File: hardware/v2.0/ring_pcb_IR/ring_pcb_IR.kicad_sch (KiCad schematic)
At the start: 22 parts, among them Q1 Q_PNP_BEC, Q2 Q_Dual_NPN_NPN_E1B1C2E2B2C1, Q3 Q_Dual_NPN_NPN_E1B1C2E2B2C1, U2 ATtiny85-20M

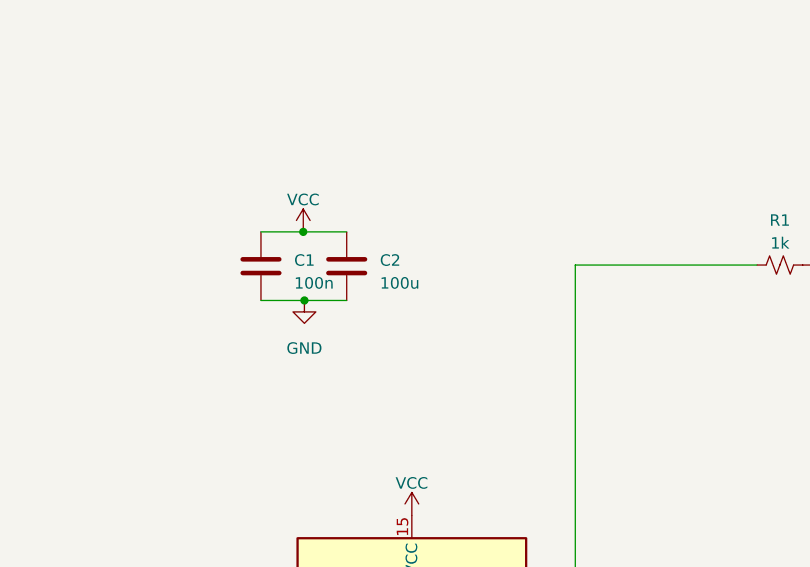
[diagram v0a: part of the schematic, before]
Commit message: New Gerbers with smaller dual-NPN
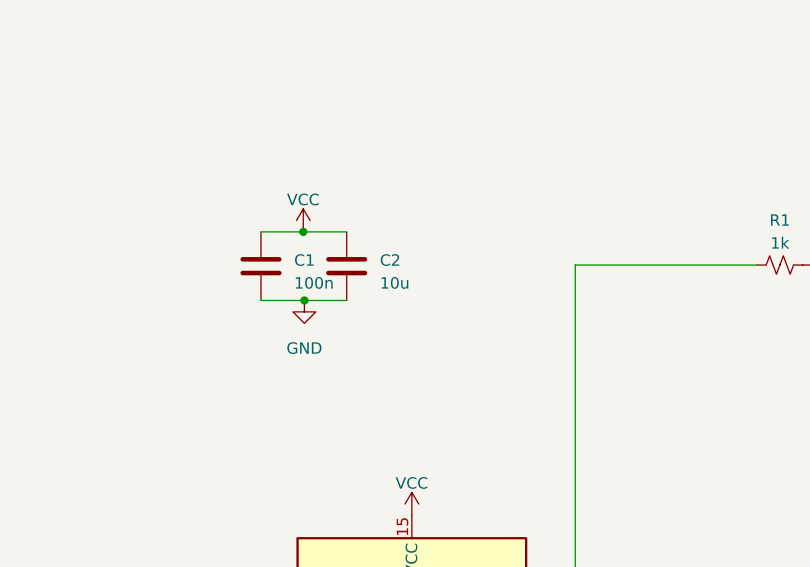
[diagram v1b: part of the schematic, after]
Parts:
- C2: value 100u -> 10u; MPN (none) -> GRM188R61A106KE69J
- Q1: MPN (none) -> MMBTA55LT1G
- TP1, TP2, TP3, TP4, TP5, TP6, TP7, TP8, TP9: MPN (none) -> DNP
- U2: MPN (none) -> ATTINY85-20MU
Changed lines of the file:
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@@
       (effects (font (size 1.27 1.27)) hide)
     )
-    (property "MPN" "" (at 87.249 138.557 0)
+    (property "MPN" "DNP" (at 87.249 138.557 0)
       (effects (font (size 1.27 1.27)) hide)
     )
@@
       (effects (font (size 1.27 1.27)) hide)
     )
-    (property "MPN" "" (at 108.839 138.43 0)
+    (property "MPN" "DNP" (at 108.839 138.43 0)
       (effects (font (size 1.27 1.27)) hide)
     )
@@
       (effects (font (size 1.27 1.27)) hide)
     )
-    (property "MPN" "" (at 87.503 147.32 0)
+    (property "MPN" "DNP" (at 87.503 147.32 0)
       (effects (font (size 1.27 1.27)) hide)
     )
@@
       (effects (font (size 1.27 1.27)) hide)
     )
-    (property "MPN" "" (at 101.473 138.43 0)
+    (property "MPN" "DNP" (at 101.473 138.43 0)
       (effects (font (size 1.27 1.27)) hide)
     )
@@
       (effects (font (size 1.27 1.27)) hide)
     )
-    (property "MPN" "" (at 112.395 103.886 0)
+    (property "MPN" "ATTINY85-20MU" (at 112.395 103.886 0)
       (effects (font (size 1.27 1.27)) hide)
     )
@@
       (effects (font (size 1.27 1.27)) hide)
     )
-    (property "MPN" "" (at 104.013 147.447 0)
+    (property "MPN" "DNP" (at 104.013 147.447 0)
       (effects (font (size 1.27 1.27)) hide)
     )
@@
       (effects (font (size 1.27 1.27)) hide)
     )
-    (property "MPN" "" (at 73.406 138.684 0)
+    (property "MPN" "DNP" (at 73.406 138.684 0)
       (effects (font (size 1.27 1.27)) hide)
     )
@@
       (effects (font (size 1.27 1.27)) (justify left))
     )
-    (property "Value" "100u" (at 108.839 62.865 0)
+    (property "Value" "10u" (at 108.839 62.865 0)
       (effects (font (size 1.27 1.27)) (justify left))
     )
@@
       (effects (font (size 1.27 1.27)) hide)
     )
-    (property "Datasheet" "~" (at 105.156 60.96 0)
-      (effects (font (size 1.27 1.27)) hide)
-    )
-    (property "MPN" "" (at 105.156 60.96 0)
+    (property "Datasheet" "https://au.mouser.com/datasheet/2/281/murata_03052018_GRM_Series_1-1310166.pdf" (at 105.156 60.96 0)
+      (effects (font (size 1.27 1.27)) hide)
+    )
+    (property "MPN" "GRM188R61A106KE69J" (at 105.156 60.96 0)
       (effects (font (size 1.27 1.27)) hide)
     )
@@
       (effects (font (size 1.27 1.27)) hide)
     )
-    (property "MPN" "" (at 58.928 147.066 0)
+    (property "MPN" "DNP" (at 58.928 147.066 0)
       (effects (font (size 1.27 1.27)) hide)
     )
@@
       (effects (font (size 1.27 1.27)) hide)
     )
-    (property "MPN" "" (at 73.406 147.32 0)
+    (property "MPN" "DNP" (at 73.406 147.32 0)
       (effects (font (size 1.27 1.27)) hide)
     )
@@
       (effects (font (size 1.27 1.27)) hide)
     )
-    (property "MPN" "" (at 59.055 138.938 0)
+    (property "MPN" "DNP" (at 59.055 138.938 0)
       (effects (font (size 1.27 1.27)) hide)
     )
@@
       (effects (font (size 1.27 1.27)) hide)
     )
-    (property "Datasheet" "~" (at 160.909 60.833 0)
-      (effects (font (size 1.27 1.27)) hide)
-    )
-    (property "MPN" "" (at 160.909 60.833 0)
-      (effects (font (size 1.27 1.27)) hide)
-    )
+    (property "Datasheet" "https://au.mouser.com/datasheet/2/308/1/MMBTA55LT1_D-2316071.pdf" (at 160.909 60.833 0)
+      (effects (font (size 1.27 1.27)) hide)
+    )
+    (property "MPN" "MMBTA55LT1G" (at 160.909 60.833 0)
+      (effects (font (size 1.27 1.27)) hide)
+    )

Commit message: Create BOM
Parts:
- TP1, TP2, TP3, TP4, TP5, TP6, TP7, TP8, TP9: DNP (none) -> DNP
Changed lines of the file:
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@@
+      (effects (font (size 1.27 1.27)) hide)
+    )
+    (property "DNP" "" (at 223.4692 29.2608 0)
       (effects (font (size 1.27 1.27)) hide)
     )
@@
       (effects (font (size 1.27 1.27)) hide)
     )
+    (property "DNP" "DNP" (at 87.249 138.557 0)
+      (effects (font (size 1.27 1.27)) hide)
+    )
     (pin "1")
     (instances
@@
       (effects (font (size 1.27 1.27)) hide)
     )
+    (property "DNP" "" (at 95.631 60.96 0)
+      (effects (font (size 1.27 1.27)) hide)
+    )
     (pin "1")
     (pin "2")
@@
       (effects (font (size 1.27 1.27)) hide)
     )
+    (property "DNP" "DNP" (at 108.839 138.43 0)
+      (effects (font (size 1.27 1.27)) hide)
+    )
     (pin "1")
     (instances
@@
       (effects (font (size 1.27 1.27)) hide)
     )
+    (property "DNP" "DNP" (at 87.503 147.32 0)
+      (effects (font (size 1.27 1.27)) hide)
+    )
     (pin "1")
     (instances
@@
       (effects (font (size 1.27 1.27)) hide)
     )
+    (property "DNP" "" (at 179.07 120.65 0)
+      (effects (font (size 1.27 1.27)) hide)
+    )
     (pin "1")
     (pin "2")
@@
     )
     (property "MPN" "BC847BS,115" (at 195.707 45.847 0)
+      (effects (font (size 1.27 1.27)) hide)
+    )
+    (property "DNP" "" (at 195.707 45.847 0)
       (effects (font (size 1.27 1.27)) hide)
     )
@@
       (effects (font (size 1.27 1.27)) hide)
     )
+    (property "DNP" "DNP" (at 101.473 138.43 0)
+      (effects (font (size 1.27 1.27)) hide)
+    )
     (pin "1")
     (instances
@@
     )
     (property "MPN" "ATTINY85-20MU" (at 112.395 103.886 0)
+      (effects (font (size 1.27 1.27)) hide)
+    )
+    (property "DNP" "" (at 112.395 103.886 0)
       (effects (font (size 1.27 1.27)) hide)
     )
@@
       (effects (font (size 1.27 1.27)) hide)
     )
+    (property "DNP" "" (at 220.853 45.593 0)
+      (effects (font (size 1.27 1.27)) hide)
+    )
     (pin "1")
     (pin "2")
@@
       (effects (font (size 1.27 1.27)) hide)
     )
+    (property "DNP" "" (at 153.289 60.833 0)
+      (effects (font (size 1.27 1.27)) hide)
+    )
     (pin "1")
     (pin "2")
@@
       (effects (font (size 1.27 1.27)) hide)
     )
+    (property "DNP" "DNP" (at 104.013 147.447 0)
+      (effects (font (size 1.27 1.27)) hide)
+    )
     (pin "1")
     (instances
@@
       (effects (font (size 1.27 1.27)) hide)
     )
+    (property "DNP" "" (at 198.1708 29.2608 0)
+      (effects (font (size 1.27 1.27)) hide)
+    )
     (pin "1")
     (pin "2")
@@
       (effects (font (size 1.27 1.27)) hide)
     )
+    (property "DNP" "DNP" (at 73.406 138.684 0)
+      (effects (font (size 1.27 1.27)) hide)
+    )
     (pin "1")
     (instances
@@
       (effects (font (size 1.27 1.27)) hide)
     )
+    (property "DNP" "" (at 223.4692 87.7824 0)
+      (effects (font (size 1.27 1.27)) hide)
+    )
     (pin "1")
     (pin "2")
@@
       (effects (font (size 1.27 1.27)) hide)
     )
+    (property "DNP" "" (at 170.561 120.65 0)
+      (effects (font (size 1.27 1.27)) hide)
+    )
     (pin "1")
     (pin "2")
@@
       (effects (font (size 1.27 1.27)) hide)
     )
+    (property "DNP" "" (at 105.156 60.96 0)
+      (effects (font (size 1.27 1.27)) hide)
+    )
     (pin "1")
     (pin "2")
@@
       (effects (font (size 1.27 1.27)) hide)
     )
+    (property "DNP" "DNP" (at 58.928 147.066 0)
+      (effects (font (size 1.27 1.27)) hide)
+    )
     (pin "1")
     (instances
@@
     )
     (property "MPN" "DNP" (at 73.406 147.32 0)
+      (effects (font (size 1.27 1.27)) hide)
+    )
+    (property "DNP" "DNP" (at 73.406 147.32 0)
       (effects (font (size 1.27 1.27)) hide)
     )
@@
       (effects (font (size 1.27 1.27)) hide)
     )
+    (property "DNP" "" (at 198.1708 87.63 0)
+      (effects (font (size 1.27 1.27)) hide)
+    )
     (pin "1")
     (pin "2")
@@
     )
     (property "MPN" "DNP" (at 59.055 138.938 0)
+      (effects (font (size 1.27 1.27)) hide)
+    )
+    (property "DNP" "DNP" (at 59.055 138.938 0)
       (effects (font (size 1.27 1.27)) hide)
     )
@@
     )
     (property "MPN" "BC847BS,115" (at 220.98 71.247 0)
+      (effects (font (size 1.27 1.27)) hide)
+    )
+    (property "DNP" "" (at 220.98 71.247 0)
       (effects (font (size 1.27 1.27)) hide)
     )
@@
       (effects (font (size 1.27 1.27)) hide)
     )
+    (property "DNP" "" (at 160.909 60.833 0)
+      (effects (font (size 1.27 1.27)) hide)
+    )
     (pin "1")
     (pin "2")
@@
       (effects (font (size 1.27 1.27)) hide)
     )
+    (property "DNP" "" (at 195.707 71.247 0)
+      (effects (font (size 1.27 1.27)) hide)
+    )
